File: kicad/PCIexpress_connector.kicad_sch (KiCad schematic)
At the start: 2 parts, among them J1 PCIexpress_bracket, J2 PCIexpress_x4

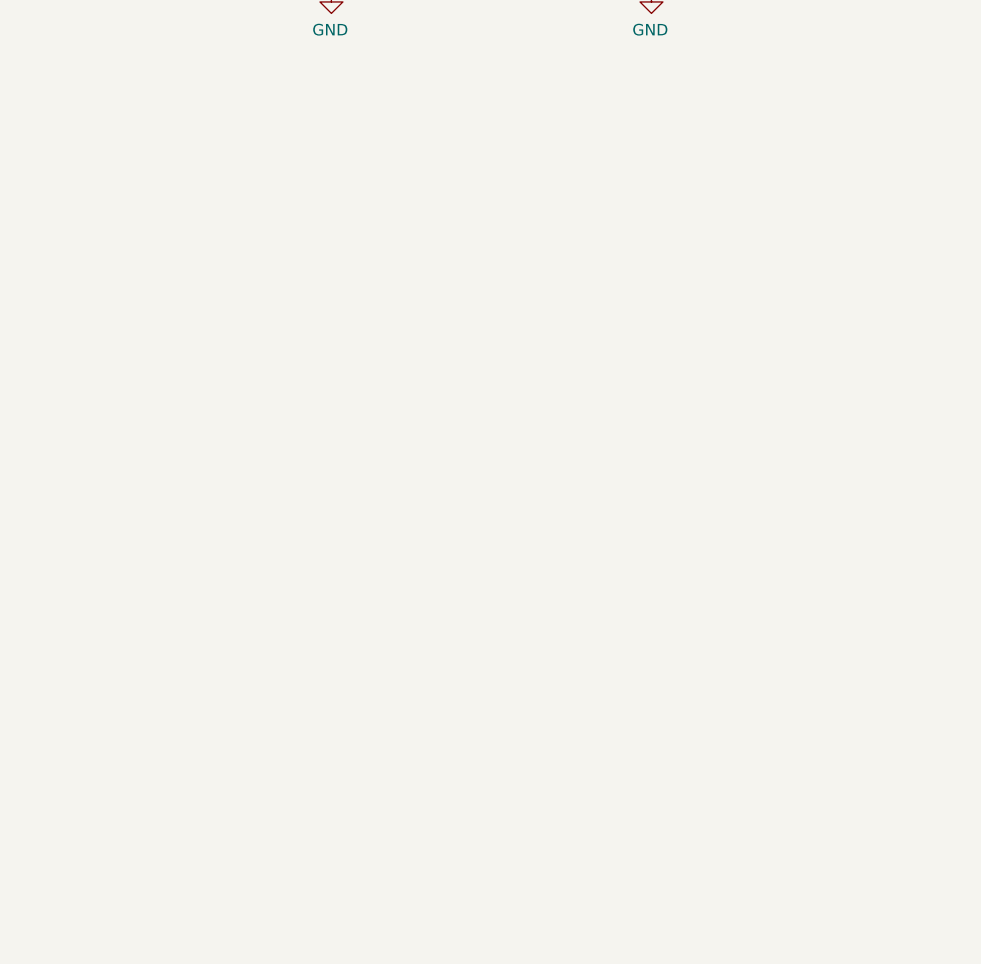
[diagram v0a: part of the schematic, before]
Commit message: Adding PCIe power connector - fix 31
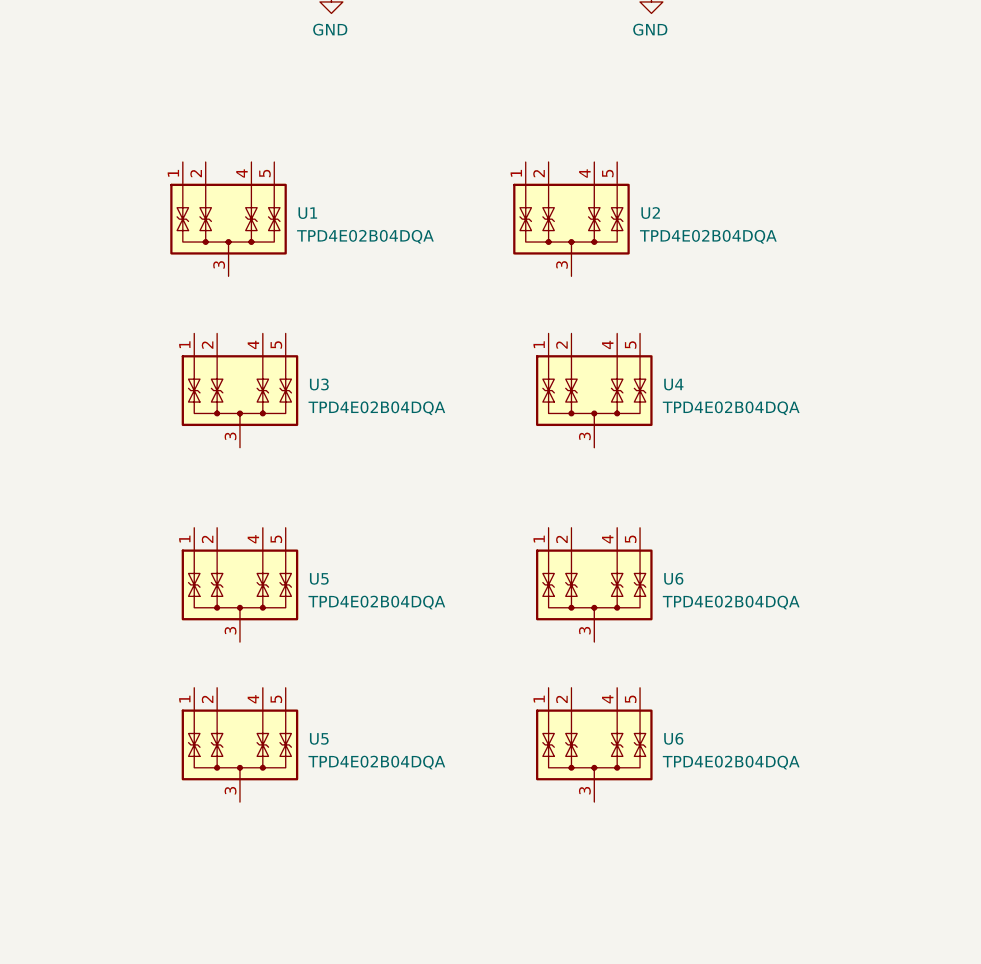
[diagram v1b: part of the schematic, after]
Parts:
- added U1, U2, U3, U4, U5 (x2), U6 (x2): TPD4E02B04DQA, Package_SON:USON-10_2.5x1.0mm_P0.5mm, symbol Power_Protection:TPD4E02B04DQA
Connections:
- new net: U6.3 (G), U6.8 (G) (x2)
- new net: U2.3 (G), U2.8 (G)
- new net: U5.3 (G), U5.8 (G) (x2)
- new net: U1.3 (G), U1.8 (G)
- new net: U4.3 (G), U4.8 (G)
- new net: U3.3 (G), U3.8 (G)

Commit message: finalising connections
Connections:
- net GND: now also U1.3 (G), U1.8 (G), U2.3 (G), U2.8 (G), U3.3 (G), U3.8 (G), U4.3 (G), U4.8 (G), U5.3 (G), U5.3 (G), U5.8 (G), U5.8 (G), U6.3 (G), U6.3 (G), U6.8 (G), U6.8 (G)
- net PER0_N: now also U3.2 (IO2)
- net PER0_P: now also U3.1 (IO1)
- net PER1_N: now also U3.5 (IO4)
- net PER1_P: now also U3.4 (IO3)
- net PER2_N: now also U4.2 (IO2)
- net PER2_P: now also U4.1 (IO1)
- net PER3_P: now also U4.4 (IO3)
- net PET0_N: now also U1.2 (IO2)
- net PET0_P: now also U1.1 (IO1)
- net PET1_N: now also U1.5 (IO4)
- net PET1_P: now also U1.4 (IO3)
- net PET2_N: now also U2.2 (IO2)
- net PET2_P: now also U2.1 (IO1)
- net PET3_N: now also U2.5 (IO4)
- net PET3_P: now also U2.4 (IO3)
- net REFCLK+: now also U5.1 (IO1)
- net REFCLK-: now also U5.2 (IO2)
- net SMCLK: now also U5.1 (IO1)
- net SMDAT: now also U5.2 (IO2)
- net TCK: now also U6.5 (IO4)
- net TDI: now also U6.4 (IO3)
- net TDO: now also U6.2 (IO2)
- net TMS: now also U6.1 (IO1)
- net ~{PERST}: now also U6.1 (IO1)
- net ~{PRSNT1}: now also U6.2 (IO2)
- net ~{PRSNT2x1}: now also U5.5 (IO4)
- net ~{PRSNT2x4}: now also U5.4 (IO3)
- net ~{TRST}: now also U6.5 (IO4)
- net ~{WAKE}: now also U6.4 (IO3)
- net PER4_N: now reaches U4.5 (IO4)
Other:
- moved on the sheet: U1, U2, U3, U4, U5, U6

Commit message: Routing PCIe
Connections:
- net PER4_N is gone; now on net PER3_N: U4.5 (IO4)
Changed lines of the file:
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@@
     (effects (font (size 1.27 1.27)) (justify left bottom))
   )
-  (label "PER4_N" (at 187.96 104.14 0) (fields_autoplaced)
+  (label "PER3_N" (at 187.96 104.14 0) (fields_autoplaced)
     (effects (font (size 1.27 1.27)) (justify left bottom))
   )

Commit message: Routing
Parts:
- U1, U2, U3, U4, U5, U6: footprint Package_SON:USON-10_2.5x1.0mm_P0.5mm -> TPD4E02:USON-10_2.5x1.0mm_P0.5mm
- U7: renamed from U5; footprint Package_SON:USON-10_2.5x1.0mm_P0.5mm -> TPD4E02:USON-10_2.5x1.0mm_P0.5mm
- U8: renamed from U6; footprint Package_SON:USON-10_2.5x1.0mm_P0.5mm -> TPD4E02:USON-10_2.5x1.0mm_P0.5mm

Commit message: uređena schema
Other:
- company: Author: Luca Anastasio -> ${project_creator}
- title: PCIexpress_x4_half -> ${project_name} ${project_version}
- moved on the sheet: J2, U1, U2, U3, U4, U5, U6, U7, U8
